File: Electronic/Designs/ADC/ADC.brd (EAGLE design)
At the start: 50 x 50 mm, 12 parts

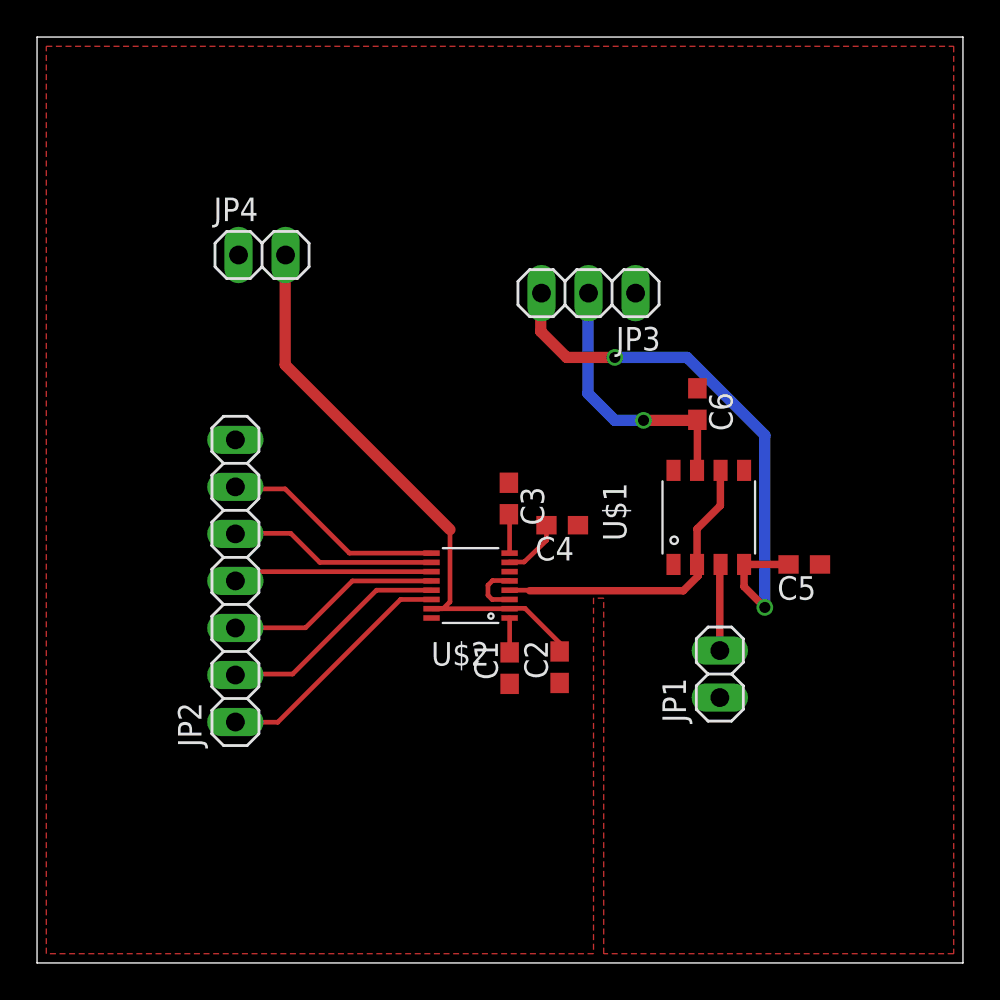
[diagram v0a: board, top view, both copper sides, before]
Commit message: Increassed isolation for ADC board, fixed DAC board isolation errors, and added mounting holes for ADC board
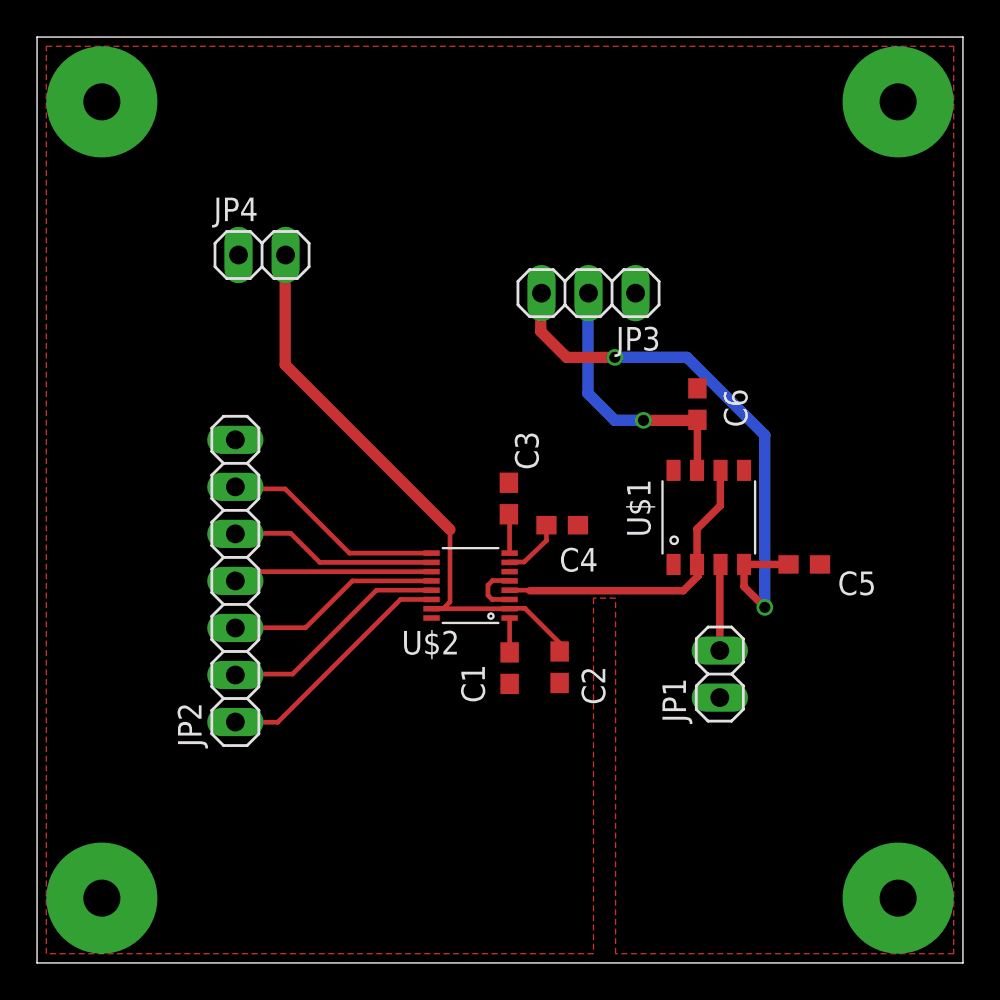
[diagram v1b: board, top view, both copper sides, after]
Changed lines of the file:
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@@
 <layer number="43" name="vRestrict" color="2" fill="10" visible="yes" active="yes"/>
 <layer number="44" name="Drills" color="7" fill="1" visible="no" active="yes"/>
-<layer number="45" name="Holes" color="7" fill="1" visible="no" active="yes"/>
+<layer number="45" name="Holes" color="7" fill="1" visible="yes" active="yes"/>
 <layer number="46" name="Milling" color="3" fill="1" visible="no" active="yes"/>
 <layer number="47" name="Measures" color="7" fill="1" visible="no" active="yes"/>
@@
 </autorouter>
 <elements>
-<element name="C1" library="resistor" package="C0603" value="100nf" x="25.52" y="15.92" rot="R90"/>
-<element name="C2" library="resistor" package="C0603" value="100nf" x="28.22" y="15.97" rot="R90"/>
-<element name="C3" library="resistor" package="C0603" value="100nf" x="25.48" y="25.08" rot="R270"/>
-<element name="C4" library="resistor" package="C0603" value="47uf" x="28.36" y="23.64" rot="R180"/>
-<element name="C5" library="resistor" package="C0603" value="100nf" x="41.43" y="21.52" rot="R180"/>
-<element name="C6" library="resistor" package="C0603" value="100nf" x="35.66" y="30.18" rot="R270"/>
+<element name="C1" library="resistor" package="C0603" value="100nf" x="25.52" y="15.92" smashed="yes" rot="R90">
+<attribute name="NAME" x="24.185" y="14.035" size="1.27" layer="25" rot="R90"/>
+<attribute name="VALUE" x="26.125" y="9.035" size="1.27" layer="27" rot="R90"/>
+</element>
+<element name="C2" library="resistor" package="C0603" value="100nf" x="28.22" y="15.97" smashed="yes" rot="R90">
+<attribute name="NAME" x="30.685" y="13.935" size="1.27" layer="25" rot="R90"/>
+<attribute name="VALUE" x="29.225" y="8.835" size="1.27" layer="27" rot="R90"/>
+</element>
+<element name="C3" library="resistor" package="C0603" value="100nf" x="25.48" y="25.08" smashed="yes" rot="R270">
+<attribute name="NAME" x="25.815" y="28.715" size="1.27" layer="25" rot="R270"/>
+<attribute name="VALUE" x="22.825" y="29.815" size="1.27" layer="27" rot="R270"/>
+</element>
+<element name="C4" library="resistor" package="C0603" value="47uf" x="28.36" y="23.64" smashed="yes" rot="R180">
+<attribute name="NAME" x="30.295" y="22.405" size="1.27" layer="25" rot="R180"/>
+<attribute name="VALUE" x="31.145" y="26.095" size="1.27" layer="27" rot="R180"/>
+</element>
+<element name="C5" library="resistor" package="C0603" value="100nf" x="41.43" y="21.52" smashed="yes" rot="R180">
+<attribute name="NAME" x="43.235" y="19.865" size="1.27" layer="25"/>
+<attribute name="VALUE" x="46.615" y="24.125" size="1.27" layer="27" rot="R180"/>
+</element>
+<element name="C6" library="resistor" package="C0603" value="100nf" x="35.66" y="30.18" smashed="yes" rot="R270">
+<attribute name="NAME" x="37.095" y="31.015" size="1.27" layer="25" rot="R270"/>
+<attribute name="VALUE" x="32.955" y="32.115" size="1.27" layer="27" rot="R270"/>
+</element>
 <element name="JP1" library="pinhead" package="1X02" value="AIN" x="36.87" y="15.6" rot="R90"/>
 <element name="JP2" library="pinhead" package="1X07" value="DOUT" x="10.71" y="20.63" rot="R90"/>
 <element name="JP3" library="pinhead" package="1X03" value="PW1" x="29.78" y="36.17" rot="R180"/>
 <element name="JP4" library="pinhead" package="1X02" value="PW2" x="12.15" y="38.23"/>
-<element name="U$1" library="LT1468" package="SOIC-8" value="LT1468" x="35.64" y="24.06" rot="R90"/>
-<element name="U$2" library="LTC2326-16" package="16-MSOP" value="LTC2326-16" x="23.41" y="20.63" rot="R180"/>
+<element name="U$1" library="LT1468" package="SOIC-8" value="LT1468" x="35.64" y="24.06" smashed="yes" rot="R90">
+<attribute name="NAME" x="33.13" y="22.99" size="1.27" layer="21" rot="R90"/>
+<attribute name="VALUE" x="40.87" y="24.14" size="1.27" layer="27" rot="R90"/>
+</element>
+<element name="U$2" library="LTC2326-16" package="16-MSOP" value="LTC2326-16" x="23.41" y="20.63" smashed="yes" rot="R180">
+<attribute name="NAME" x="22.826" y="17.928" size="1.27" layer="21" rot="R180"/>
+<attribute name="VALUE" x="24.042" y="24.044" size="1.27" layer="27" rot="R180"/>
+</element>
 </elements>
 <signals>
@@
 <contactref element="JP3" pad="1"/>
 <contactref element="JP4" pad="1"/>
-<polygon width="0.254" layer="1">
+<polygon width="0.254" layer="1" isolate="0.3048">
 <vertex x="0.5" y="49.5"/>
 <vertex x="49.5" y="49.5"/>
 <vertex x="49.5" y="0.5"/>
-<vertex x="30.6" y="0.5"/>
-<vertex x="30.6" y="19.7"/>
-<vertex x="30.05" y="19.7"/>
-<vertex x="30.05" y="0.5"/>
+<vertex x="31.242" y="0.5"/>
+<vertex x="31.242" y="19.7"/>
+<vertex x="30.0482" y="19.7"/>
+<vertex x="30.0482" y="0.5"/>
 <vertex x="0.5" y="0.5"/>
 </polygon>
@@
 <wire x1="10.82" y1="25.6" x2="10.71" y2="25.71" width="0.254" layer="1"/>
 </signal>
+<signal name="MOUNT">
+<via x="3.5" y="46.5" extent="1-16" drill="2" diameter="6"/>
+<via x="46.5" y="46.5" extent="1-16" drill="2" diameter="6"/>
+<via x="46.5" y="3.5" extent="1-16" drill="2" diameter="6"/>
+<via x="3.5" y="3.5" extent="1-16" drill="2" diameter="6"/>
+<wire x1="3.5" y1="46.5" x2="46.5" y2="46.5" width="0" layer="19" extent="1-1"/>
+<wire x1="46.5" y1="3.5" x2="46.5" y2="46.5" width="0" layer="19" extent="1-1"/>
+<wire x1="3.5" y1="3.5" x2="3.5" y2="46.5" width="0" layer="19" extent="1-1"/>
+</signal>
 </signals>

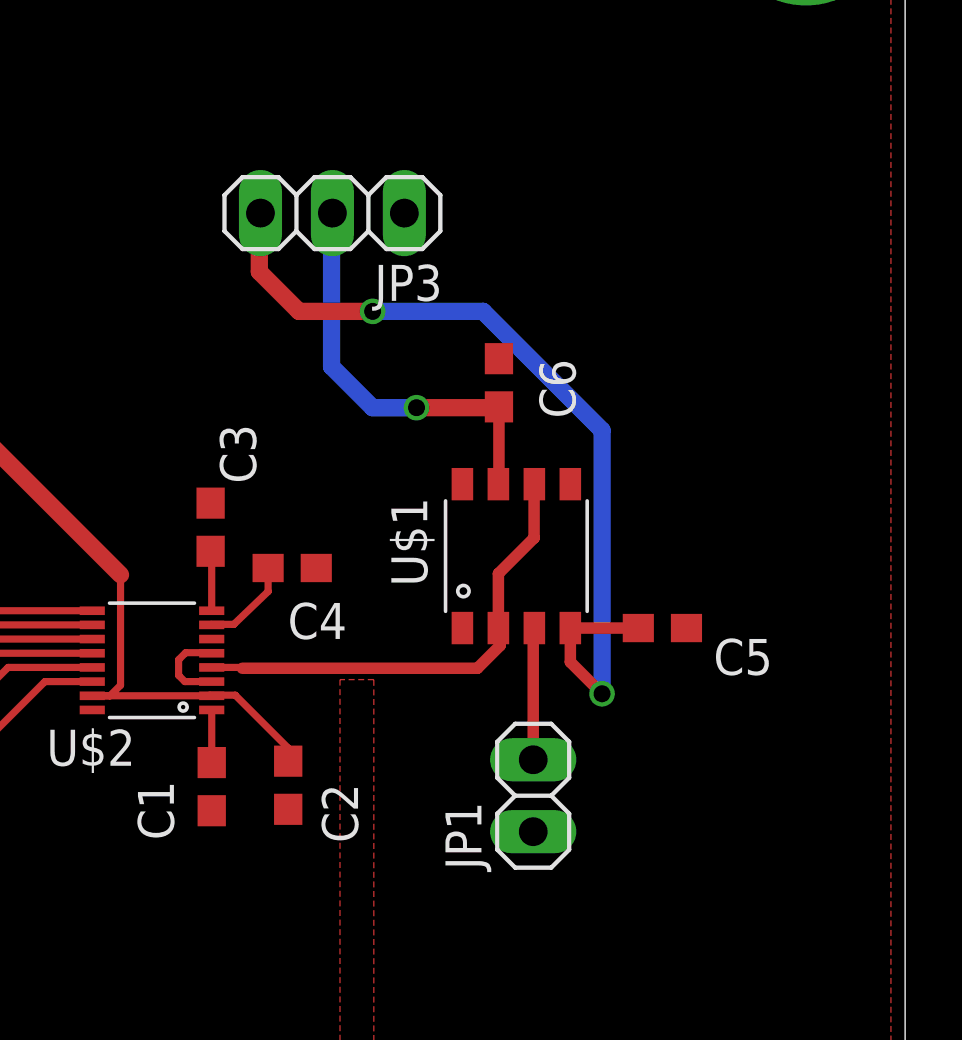
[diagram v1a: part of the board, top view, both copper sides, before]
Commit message: reduced path of analogue signal from opamp to adc
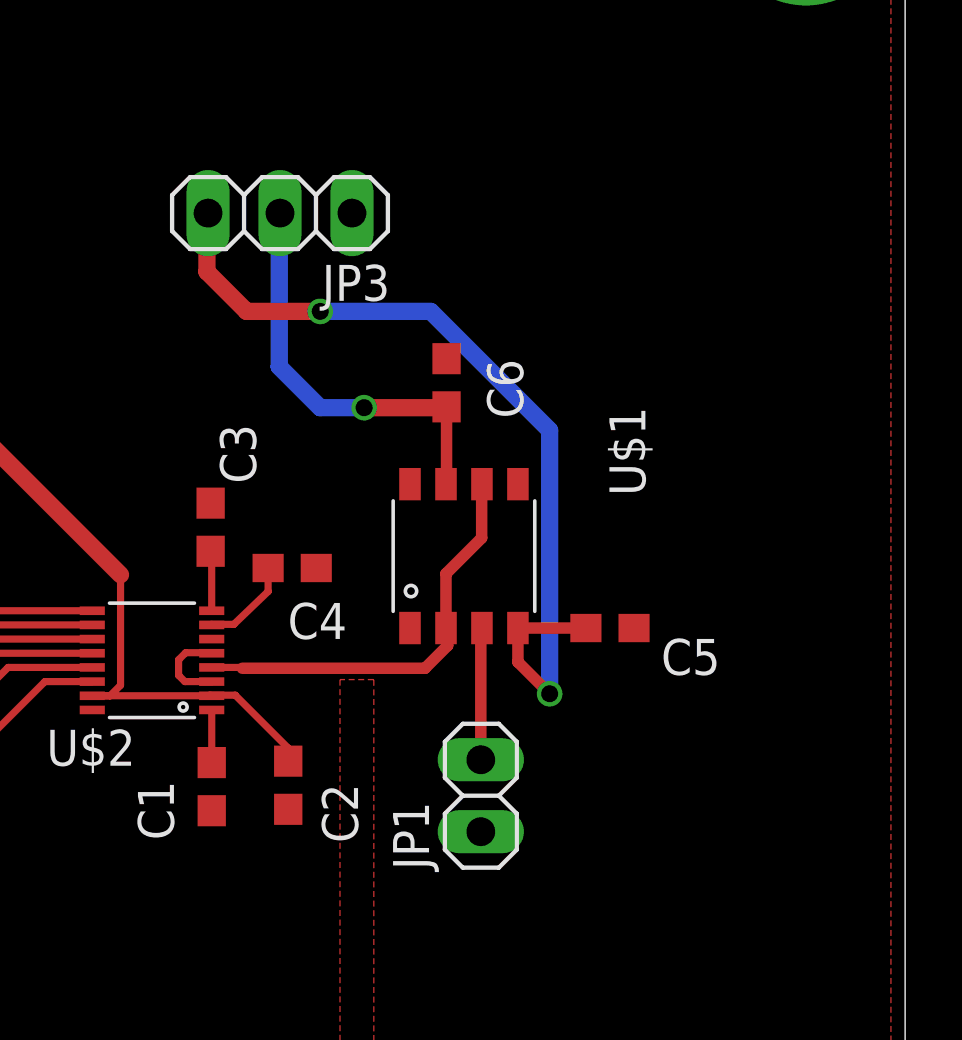
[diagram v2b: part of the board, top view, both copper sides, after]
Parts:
- moved C5 1.85 mm to (39.6, 21.5)
- moved JP3 1.85 mm to (27.9, 36.2)
- moved U$1 1.85 mm to (33.8, 24.1)
- moved C6 1.85 mm to (33.8, 30.2)
- moved JP1 1.85 mm to (35.0, 15.6)
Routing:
- net N$1: track 16.8 -> 14.9 mm
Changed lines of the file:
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@@
 <setting verticaltext="up"/>
 </settings>
-<grid distance="0.05" unitdist="mm" unit="mm" style="lines" multiple="1" display="no" altdistance="0.025" altunitdist="inch" altunit="mm"/>
+<grid distance="0.0500000001" unitdist="mm" unit="mm" style="lines" multiple="1" display="no" altdistance="0.025" altunitdist="inch" altunit="mm"/>
 <layers>
 <layer number="1" name="Top" color="4" fill="1" visible="yes" active="yes"/>
@@
 <element name="C4" library="resistor" package="C0603" value="47uf" x="28.36" y="23.64" smashed="yes" rot="R180">
 <attribute name="NAME" x="30.295" y="22.405" size="1.27" layer="25" rot="R180"/>
-<attribute name="VALUE" x="31.145" y="26.095" size="1.27" layer="27" rot="R180"/>
-</element>
-<element name="C5" library="resistor" package="C0603" value="100nf" x="41.43" y="21.52" smashed="yes" rot="R180">
-<attribute name="NAME" x="43.235" y="19.865" size="1.27" layer="25"/>
-<attribute name="VALUE" x="46.615" y="24.125" size="1.27" layer="27" rot="R180"/>
-</element>
-<element name="C6" library="resistor" package="C0603" value="100nf" x="35.66" y="30.18" smashed="yes" rot="R270">
-<attribute name="NAME" x="37.095" y="31.015" size="1.27" layer="25" rot="R270"/>
-<attribute name="VALUE" x="32.955" y="32.115" size="1.27" layer="27" rot="R270"/>
-</element>
-<element name="JP1" library="pinhead" package="1X02" value="AIN" x="36.87" y="15.6" rot="R90"/>
+<attribute name="VALUE" x="30.545" y="26.095" size="1.27" layer="27" rot="R180"/>
+</element>
+<element name="C5" library="resistor" package="C0603" value="100nf" x="39.58" y="21.52" smashed="yes" rot="R180">
+<attribute name="NAME" x="41.385" y="19.865" size="1.27" layer="25"/>
+<attribute name="VALUE" x="44.765" y="24.125" size="1.27" layer="27" rot="R180"/>
+</element>
+<element name="C6" library="resistor" package="C0603" value="100nf" x="33.81" y="30.18" smashed="yes" rot="R270">
+<attribute name="NAME" x="35.245" y="31.015" size="1.27" layer="25" rot="R270"/>
+<attribute name="VALUE" x="31.105" y="32.115" size="1.27" layer="27" rot="R270"/>
+</element>
+<element name="JP1" library="pinhead" package="1X02" value="AIN" x="35.02" y="15.6" rot="R90"/>
 <element name="JP2" library="pinhead" package="1X07" value="DOUT" x="10.71" y="20.63" rot="R90"/>
-<element name="JP3" library="pinhead" package="1X03" value="PW1" x="29.78" y="36.17" rot="R180"/>
+<element name="JP3" library="pinhead" package="1X03" value="PW1" x="27.93" y="36.17" rot="R180"/>
 <element name="JP4" library="pinhead" package="1X02" value="PW2" x="12.15" y="38.23"/>
-<element name="U$1" library="LT1468" package="SOIC-8" value="LT1468" x="35.64" y="24.06" smashed="yes" rot="R90">
-<attribute name="NAME" x="33.13" y="22.99" size="1.27" layer="21" rot="R90"/>
-<attribute name="VALUE" x="40.87" y="24.14" size="1.27" layer="27" rot="R90"/>
+<element name="U$1" library="LT1468" package="SOIC-8" value="LT1468" x="33.79" y="24.06" smashed="yes" rot="R90">
+<attribute name="NAME" x="40.83" y="26.19" size="1.27" layer="21" rot="R90"/>
+<attribute name="VALUE" x="39.02" y="24.14" size="1.27" layer="27" rot="R90"/>
 </element>
 <element name="U$2" library="LTC2326-16" package="16-MSOP" value="LTC2326-16" x="23.41" y="20.63" smashed="yes" rot="R180">
@@
 <wire x1="25.5182" y1="20.12961875" x2="26.57038125" y2="20.12961875" width="0.254" layer="1"/>
 <wire x1="26.57038125" y1="20.12961875" x2="26.6" y2="20.1" width="0.254" layer="1"/>
-<wire x1="26.6" y1="20.1" x2="34.9" y2="20.1" width="0.4064" layer="1"/>
-<wire x1="34.9" y1="20.1" x2="35.7" y2="20.9" width="0.4064" layer="1"/>
-<wire x1="35.7" y1="20.9" x2="35.7" y2="21.46" width="0.4064" layer="1"/>
-<wire x1="35.7" y1="21.46" x2="35.64" y2="21.52" width="0.4064" layer="1"/>
-<wire x1="35.64" y1="21.52" x2="35.64" y2="23.44" width="0.4064" layer="1"/>
-<wire x1="35.64" y1="23.44" x2="36.9" y2="24.7" width="0.4064" layer="1"/>
-<wire x1="36.9" y1="24.7" x2="36.9" y2="26.59" width="0.4064" layer="1"/>
-<wire x1="36.9" y1="26.59" x2="36.91" y2="26.6" width="0.4064" layer="1"/>
+<wire x1="26.6" y1="20.1" x2="33.05" y2="20.1" width="0.4064" layer="1"/>
+<wire x1="33.05" y1="20.1" x2="33.85" y2="20.9" width="0.4064" layer="1"/>
+<wire x1="33.85" y1="20.9" x2="33.85" y2="21.46" width="0.4064" layer="1"/>
+<wire x1="33.85" y1="21.46" x2="33.79" y2="21.52" width="0.4064" layer="1"/>
+<wire x1="33.79" y1="21.52" x2="33.79" y2="23.44" width="0.4064" layer="1"/>
+<wire x1="33.79" y1="23.44" x2="35.05" y2="24.7" width="0.4064" layer="1"/>
+<wire x1="35.05" y1="24.7" x2="35.05" y2="26.59" width="0.4064" layer="1"/>
+<wire x1="35.05" y1="26.59" x2="35.06" y2="26.6" width="0.4064" layer="1"/>
 </signal>
 <signal name="GND">
@@
 <contactref element="U$1" pad="P$4"/>
 <contactref element="JP3" pad="3"/>
-<wire x1="40.58" y1="21.52" x2="38.18" y2="21.52" width="0.4064" layer="1"/>
-<wire x1="38.18" y1="21.52" x2="38.18" y2="20.32" width="0.4064" layer="1"/>
-<wire x1="38.18" y1="20.32" x2="39.3" y2="19.2" width="0.4064" layer="1"/>
-<via x="39.3" y="19.2" extent="1-16" drill="0.6"/>
-<wire x1="39.3" y1="19.2" x2="39.3" y2="28.5" width="0.6096" layer="16"/>
-<wire x1="39.3" y1="28.5" x2="35.1" y2="32.7" width="0.6096" layer="16"/>
-<wire x1="35.1" y1="32.7" x2="31.2" y2="32.7" width="0.6096" layer="16"/>
-<via x="31.2" y="32.7" extent="1-16" drill="0.6"/>
-<wire x1="31.2" y1="32.7" x2="28.6" y2="32.7" width="0.6096" layer="1"/>
-<wire x1="28.6" y1="32.7" x2="27.2" y2="34.1" width="0.6096" layer="1"/>
-<wire x1="27.2" y1="34.1" x2="27.2" y2="36.13" width="0.6096" layer="1"/>
-<wire x1="27.2" y1="36.13" x2="27.24" y2="36.17" width="0.4064" layer="1"/>
+<wire x1="38.73" y1="21.52" x2="36.33" y2="21.52" width="0.4064" layer="1"/>
+<wire x1="36.33" y1="21.52" x2="36.33" y2="20.32" width="0.4064" layer="1"/>
+<wire x1="36.33" y1="20.32" x2="37.45" y2="19.2" width="0.4064" layer="1"/>
+<via x="37.45" y="19.2" extent="1-16" drill="0.6"/>
+<wire x1="37.45" y1="19.2" x2="37.45" y2="28.5" width="0.6096" layer="16"/>
+<wire x1="37.45" y1="28.5" x2="33.25" y2="32.7" width="0.6096" layer="16"/>
+<wire x1="33.25" y1="32.7" x2="29.35" y2="32.7" width="0.6096" layer="16"/>
+<via x="29.35" y="32.7" extent="1-16" drill="0.6"/>
+<wire x1="29.35" y1="32.7" x2="26.75" y2="32.7" width="0.6096" layer="1"/>
+<wire x1="26.75" y1="32.7" x2="25.35" y2="34.1" width="0.6096" layer="1"/>
+<wire x1="25.35" y1="34.1" x2="25.35" y2="36.13" width="0.6096" layer="1"/>
+<wire x1="25.35" y1="36.13" x2="25.39" y2="36.17" width="0.4064" layer="1"/>
 </signal>
 <signal name="+15V">
@@
 <contactref element="U$1" pad="P$7"/>
 <contactref element="JP3" pad="2"/>
-<wire x1="35.66" y1="29.33" x2="35.66" y2="26.62" width="0.4064" layer="1"/>
-<wire x1="35.66" y1="26.62" x2="35.64" y2="26.6" width="0.4064" layer="1"/>
-<via x="32.75" y="29.3" extent="1-16" drill="0.6"/>
-<wire x1="32.75" y1="29.3" x2="31.2" y2="29.3" width="0.6096" layer="16"/>
-<wire x1="31.2" y1="29.3" x2="29.75" y2="30.75" width="0.6096" layer="16"/>
-<wire x1="29.75" y1="30.75" x2="29.75" y2="36.14" width="0.6096" layer="16"/>
-<wire x1="29.75" y1="36.14" x2="29.78" y2="36.17" width="0.4064" layer="16"/>
-<wire x1="32.75" y1="29.3" x2="35.63" y2="29.3" width="0.6096" layer="1"/>
-<wire x1="35.63" y1="29.3" x2="35.66" y2="29.33" width="0.6096" layer="1"/>
+<wire x1="33.81" y1="29.33" x2="33.81" y2="26.62" width="0.4064" layer="1"/>
+<wire x1="33.81" y1="26.62" x2="33.79" y2="26.6" width="0.4064" layer="1"/>
+<via x="30.9" y="29.3" extent="1-16" drill="0.6"/>
+<wire x1="30.9" y1="29.3" x2="29.35" y2="29.3" width="0.6096" layer="16"/>
+<wire x1="29.35" y1="29.3" x2="27.9" y2="30.75" width="0.6096" layer="16"/>
+<wire x1="27.9" y1="30.75" x2="27.9" y2="36.14" width="0.6096" layer="16"/>
+<wire x1="27.9" y1="36.14" x2="27.93" y2="36.17" width="0.4064" layer="16"/>
+<wire x1="30.9" y1="29.3" x2="33.78" y2="29.3" width="0.6096" layer="1"/>
+<wire x1="33.78" y1="29.3" x2="33.81" y2="29.33" width="0.6096" layer="1"/>
 </signal>
 <signal name="N$2">
@@
 <contactref element="U$1" pad="P$3"/>
 <contactref element="JP1" pad="2"/>
-<wire x1="36.87" y1="16.87" x2="36.87" y2="21.48" width="0.4064" layer="1"/>
-<wire x1="36.87" y1="21.48" x2="36.91" y2="21.52" width="0.4064" layer="1"/>
+<wire x1="35.02" y1="16.87" x2="35.02" y2="21.48" width="0.4064" layer="1"/>
+<wire x1="35.02" y1="21.48" x2="35.06" y2="21.52" width="0.4064" layer="1"/>
 </signal>
 <signal name="CHAIN">
